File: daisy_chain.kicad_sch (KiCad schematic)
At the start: 21 parts, among them U1 BQ79616PAPRQ1, U2 SM91502ALA-E, U3 SM91502ALA-E

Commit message: PCB[Grounding, Heat]: Added some more pours for heat considerations for bjt, stiched more vias for heat consideration on balanace resistors. SCH[Notes, Block Diagram]: Working on spelling and notes updates, started block diagram.
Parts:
- renumbered C39 to C37, C40 to C38, C37 to C39, C38 to C40, C42 to C41, C41 to C42, CR2 to CR1, CR1 to CR2, R40 to R39, R39 to R40, R43 to R41, R44 to R42, R41 to R43, R42 to R44, U3 to U2, U2 to U3
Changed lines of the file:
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@@
 		(in_pos_files yes)
 		(dnp no)
-		(property "Reference" "#PWR041"
+		(property "Reference" "#PWR048"
 			(at 58.42 50.8 0)
 			(hide yes)
@@
 			(project "bms_slave"
 				(path "/f9e05184-c88b-4a88-ae9c-ab2bdb32be7c/c5103ceb-5325-4a84-a025-9638a412984e/f0b77e72-3d76-4cd4-bd9c-26bca4deb7f1"
-					(reference "#PWR041")
+					(reference "#PWR048")
 					(unit 1)
 				)
@@
 		(dnp no)
 		(fields_autoplaced yes)
-		(property "Reference" "C39"
+		(property "Reference" "C37"
 			(at 127 58.4199 90)
 			(show_name no)
@@
 			(project "bms_slave"
 				(path "/f9e05184-c88b-4a88-ae9c-ab2bdb32be7c/c5103ceb-5325-4a84-a025-9638a412984e/f0b77e72-3d76-4cd4-bd9c-26bca4deb7f1"
-					(reference "C39")
+					(reference "C37")
 					(unit 1)
 				)
@@
 		(dnp no)
 		(fields_autoplaced yes)
-		(property "Reference" "#PWR044"
+		(property "Reference" "#PWR053"
 			(at 124.46 119.38 0)
 			(hide yes)
@@
 			(project "bms_slave"
 				(path "/f9e05184-c88b-4a88-ae9c-ab2bdb32be7c/c5103ceb-5325-4a84-a025-9638a412984e/f0b77e72-3d76-4cd4-bd9c-26bca4deb7f1"
-					(reference "#PWR044")
+					(reference "#PWR053")
 					(unit 1)
 				)
@@
 		(dnp no)
 		(fields_autoplaced yes)
-		(property "Reference" "#PWR045"
+		(property "Reference" "#PWR054"
 			(at 124.46 139.7 0)
 			(hide yes)
@@
 			(project "bms_slave"
 				(path "/f9e05184-c88b-4a88-ae9c-ab2bdb32be7c/c5103ceb-5325-4a84-a025-9638a412984e/f0b77e72-3d76-4cd4-bd9c-26bca4deb7f1"
-					(reference "#PWR045")
+					(reference "#PWR054")
 					(unit 1)
 				)
@@
 		(dnp no)
 		(fields_autoplaced yes)
-		(property "Reference" "#PWR048"
+		(property "Reference" "#PWR056"
 			(at 165.1 119.38 0)
 			(hide yes)
@@
 			(project "bms_slave"
 				(path "/f9e05184-c88b-4a88-ae9c-ab2bdb32be7c/c5103ceb-5325-4a84-a025-9638a412984e/f0b77e72-3d76-4cd4-bd9c-26bca4deb7f1"
-					(reference "#PWR048")
+					(reference "#PWR056")
 					(unit 1)
 				)
@@
 		(dnp no)
 		(fields_autoplaced yes)
-		(property "Reference" "U2"
+		(property "Reference" "U3"
 			(at 203.2 97.79 0)
 			(show_name no)
@@
 			(project "bms_slave"
 				(path "/f9e05184-c88b-4a88-ae9c-ab2bdb32be7c/c5103ceb-5325-4a84-a025-9638a412984e/f0b77e72-3d76-4cd4-bd9c-26bca4deb7f1"
-					(reference "U2")
+					(reference "U3")
 					(unit 1)
 				)
@@
 		(in_pos_files yes)
 		(dnp no)
-		(property "Reference" "CR2"
+		(property "Reference" "CR1"
 			(at 153.67 57.15 0)
 			(show_name no)
@@
 			(project "bms_slave"
 				(path "/f9e05184-c88b-4a88-ae9c-ab2bdb32be7c/c5103ceb-5325-4a84-a025-9638a412984e/f0b77e72-3d76-4cd4-bd9c-26bca4deb7f1"
-					(reference "CR2")
+					(reference "CR1")
 					(unit 1)
 				)
@@
 		(dnp no)
 		(fields_autoplaced yes)
-		(property "Reference" "C40"
+		(property "Reference" "C38"
 			(at 127 78.7399 90)
 			(show_name no)
@@
 			(project "bms_slave"
 				(path "/f9e05184-c88b-4a88-ae9c-ab2bdb32be7c/c5103ceb-5325-4a84-a025-9638a412984e/f0b77e72-3d76-4cd4-bd9c-26bca4deb7f1"
-					(reference "C40")
+					(reference "C38")
 					(unit 1)
 				)
@@
 		(dnp no)
 		(fields_autoplaced yes)
-		(property "Reference" "C37"
+		(property "Reference" "C39"
 			(at 127 105.4099 90)
 			(show_name no)
@@
 			(project "bms_slave"
 				(path "/f9e05184-c88b-4a88-ae9c-ab2bdb32be7c/c5103ceb-5325-4a84-a025-9638a412984e/f0b77e72-3d76-4cd4-bd9c-26bca4deb7f1"
-					(reference "C37")
+					(reference "C39")
 					(unit 1)
 				)
@@
 		(in_pos_files yes)
 		(dnp no)
-		(property "Reference" "R39"
+		(property "Reference" "R40"
 			(at 116.84 107.9499 90)
 			(show_name no)
@@
 			(project "bms_slave"
 				(path "/f9e05184-c88b-4a88-ae9c-ab2bdb32be7c/c5103ceb-5325-4a84-a025-9638a412984e/f0b77e72-3d76-4cd4-bd9c-26bca4deb7f1"
-					(reference "R39")
+					(reference "R40")
 					(unit 1)
 				)
@@
 		(in_pos_files yes)
 		(dnp no)
-		(property "Reference" "C42"
+		(property "Reference" "C41"
 			(at 171.45 59.69 0)
 			(show_name no)
@@
 			(project "bms_slave"
 				(path "/f9e05184-c88b-4a88-ae9c-ab2bdb32be7c/c5103ceb-5325-4a84-a025-9638a412984e/f0b77e72-3d76-4cd4-bd9c-26bca4deb7f1"
-					(reference "C42")
+					(reference "C41")
 					(unit 1)
 				)
@@
 		(dnp no)
 		(fields_autoplaced yes)
-		(property "Reference" "C38"
+		(property "Reference" "C40"
 			(at 127 125.7299 90)
 			(show_name no)
@@
 			(project "bms_slave"
 				(path "/f9e05184-c88b-4a88-ae9c-ab2bdb32be7c/c5103ceb-5325-4a84-a025-9638a412984e/f0b77e72-3d76-4cd4-bd9c-26bca4deb7f1"
-					(reference "C38")
+					(reference "C40")
 					(unit 1)
 				)
@@
 		(dnp no)
 		(fields_autoplaced yes)
-		(property "Reference" "#PWR047"
+		(property "Reference" "#PWR052"
 			(at 124.46 92.71 0)
 			(hide yes)
@@
 			(project "bms_slave"
 				(path "/f9e05184-c88b-4a88-ae9c-ab2bdb32be7c/c5103ceb-5325-4a84-a025-9638a412984e/f0b77e72-3d76-4cd4-bd9c-26bca4deb7f1"
-					(reference "#PWR047")
+					(reference "#PWR052")
 					(unit 1)
 				)
@@
 		(in_pos_files yes)
 		(dnp no)
-		(property "Reference" "C41"
+		(property "Reference" "C42"
 			(at 171.45 106.68 0)
 			(show_name no)
@@
 			(project "bms_slave"
 				(path "/f9e05184-c88b-4a88-ae9c-ab2bdb32be7c/c5103ceb-5325-4a84-a025-9638a412984e/f0b77e72-3d76-4cd4-bd9c-26bca4deb7f1"
-					(reference "C41")
+					(reference "C42")
 					(unit 1)
 				)
@@
 		(dnp no)
 		(fields_autoplaced yes)
-		(property "Reference" "R42"
+		(property "Reference" "R44"
 			(at 135.89 114.3 0)
 			(show_name no)
@@
 			(project "bms_slave"
 				(path "/f9e05184-c88b-4a88-ae9c-ab2bdb32be7c/c5103ceb-5325-4a84-a025-9638a412984e/f0b77e72-3d76-4cd4-bd9c-26bca4deb7f1"
-					(reference "R42")
+					(reference "R44")
 					(unit 1)
 				)
@@
 		(dnp no)
 		(fields_autoplaced yes)
-		(property "Reference" "R43"
+		(property "Reference" "R41"
 			(at 135.89 46.99 0)
 			(show_name no)
@@
 			(project "bms_slave"
 				(path "/f9e05184-c88b-4a88-ae9c-ab2bdb32be7c/c5103ceb-5325-4a84-a025-9638a412984e/f0b77e72-3d76-4cd4-bd9c-26bca4deb7f1"
-					(reference "R43")
+					(reference "R41")
 					(unit 1)
 				)
@@
 		(dnp no)
 		(fields_autoplaced yes)
-		(property "Reference" "#PWR046"
+		(property "Reference" "#PWR051"
 			(at 124.46 72.39 0)
 			(hide yes)
@@
 			(project "bms_slave"
 				(path "/f9e05184-c88b-4a88-ae9c-ab2bdb32be7c/c5103ceb-5325-4a84-a025-9638a412984e/f0b77e72-3d76-4cd4-bd9c-26bca4deb7f1"
-					(reference "#PWR046")
+					(reference "#PWR051")
 					(unit 1)
 				)
@@
 		(in_pos_files yes)
 		(dnp no)
-		(property "Reference" "R40"
+		(property "Reference" "R39"
 			(at 116.84 60.9599 90)
 			(show_name no)
@@
 			(project "bms_slave"
 				(path "/f9e05184-c88b-4a88-ae9c-ab2bdb32be7c/c5103ceb-5325-4a84-a025-9638a412984e/f0b77e72-3d76-4cd4-bd9c-26bca4deb7f1"
-					(reference "R40")
+					(reference "R39")
 					(unit 1)
 				)
@@
 		(dnp no)
 		(fields_autoplaced yes)
-		(property "Reference" "#PWR049"
+		(property "Reference" "#PWR055"
 			(at 165.1 72.39 0)
 			(hide yes)
@@
 			(project "bms_slave"
 				(path "/f9e05184-c88b-4a88-ae9c-ab2bdb32be7c/c5103ceb-5325-4a84-a025-9638a412984e/f0b77e72-3d76-4cd4-bd9c-26bca4deb7f1"
-					(reference "#PWR049")
+					(reference "#PWR055")
 					(unit 1)
 				)
@@
 		(in_pos_files yes)
 		(dnp no)
-		(property "Reference" "CR1"
+		(property "Reference" "CR2"
 			(at 153.67 104.14 0)
 			(show_name no)
@@
 			(project "bms_slave"
 				(path "/f9e05184-c88b-4a88-ae9c-ab2bdb32be7c/c5103ceb-5325-4a84-a025-9638a412984e/f0b77e72-3d76-4cd4-bd9c-26bca4deb7f1"
-					(reference "CR1")
+					(reference "CR2")
 					(unit 1)
 				)
@@
 		(in_pos_files yes)
 		(dnp no)
-		(property "Reference" "#PWR042"
+		(property "Reference" "#PWR049"
 			(at 58.42 59.69 0)
 			(hide yes)
@@
 			(project "bms_slave"
 				(path "/f9e05184-c88b-4a88-ae9c-ab2bdb32be7c/c5103ceb-5325-4a84-a025-9638a412984e/f0b77e72-3d76-4cd4-bd9c-26bca4deb7f1"
-					(reference "#PWR042")
+					(reference "#PWR049")
 					(unit 1)
 				)
@@
 		(dnp no)
 		(fields_autoplaced yes)
-		(property "Reference" "R44"
+		(property "Reference" "R42"
 			(at 135.89 67.31 0)
 			(show_name no)
@@
 			(project "bms_slave"
 				(path "/f9e05184-c88b-4a88-ae9c-ab2bdb32be7c/c5103ceb-5325-4a84-a025-9638a412984e/f0b77e72-3d76-4cd4-bd9c-26bca4deb7f1"
-					(reference "R44")
+					(reference "R42")
 					(unit 1)
 				)
@@
 		(dnp no)
 		(fields_autoplaced yes)
-		(property "Reference" "R41"
+		(property "Reference" "R43"
 			(at 135.89 93.98 0)
 			(show_name no)
@@
 			(project "bms_slave"
 				(path "/f9e05184-c88b-4a88-ae9c-ab2bdb32be7c/c5103ceb-5325-4a84-a025-9638a412984e/f0b77e72-3d76-4cd4-bd9c-26bca4deb7f1"
-					(reference "R41")
+					(reference "R43")
 					(unit 1)
 				)
@@
 		(in_pos_files yes)
 		(dnp no)
-		(property "Reference" "#PWR043"
+		(property "Reference" "#PWR050"
 			(at 81.28 95.25 0)
 			(hide yes)
@@
 			(project "bms_slave"
 				(path "/f9e05184-c88b-4a88-ae9c-ab2bdb32be7c/c5103ceb-5325-4a84-a025-9638a412984e/f0b77e72-3d76-4cd4-bd9c-26bca4deb7f1"
-					(reference "#PWR043")
+					(reference "#PWR050")
 					(unit 1)
 				)
@@
 		(dnp no)
 		(fields_autoplaced yes)
-		(property "Reference" "U3"
+		(property "Reference" "U2"
 			(at 203.2 50.8 0)
 			(show_name no)
@@
 			(project "bms_slave"
 				(path "/f9e05184-c88b-4a88-ae9c-ab2bdb32be7c/c5103ceb-5325-4a84-a025-9638a412984e/f0b77e72-3d76-4cd4-bd9c-26bca4deb7f1"
-					(reference "U3")
+					(reference "U2")
 					(unit 1)
 				)

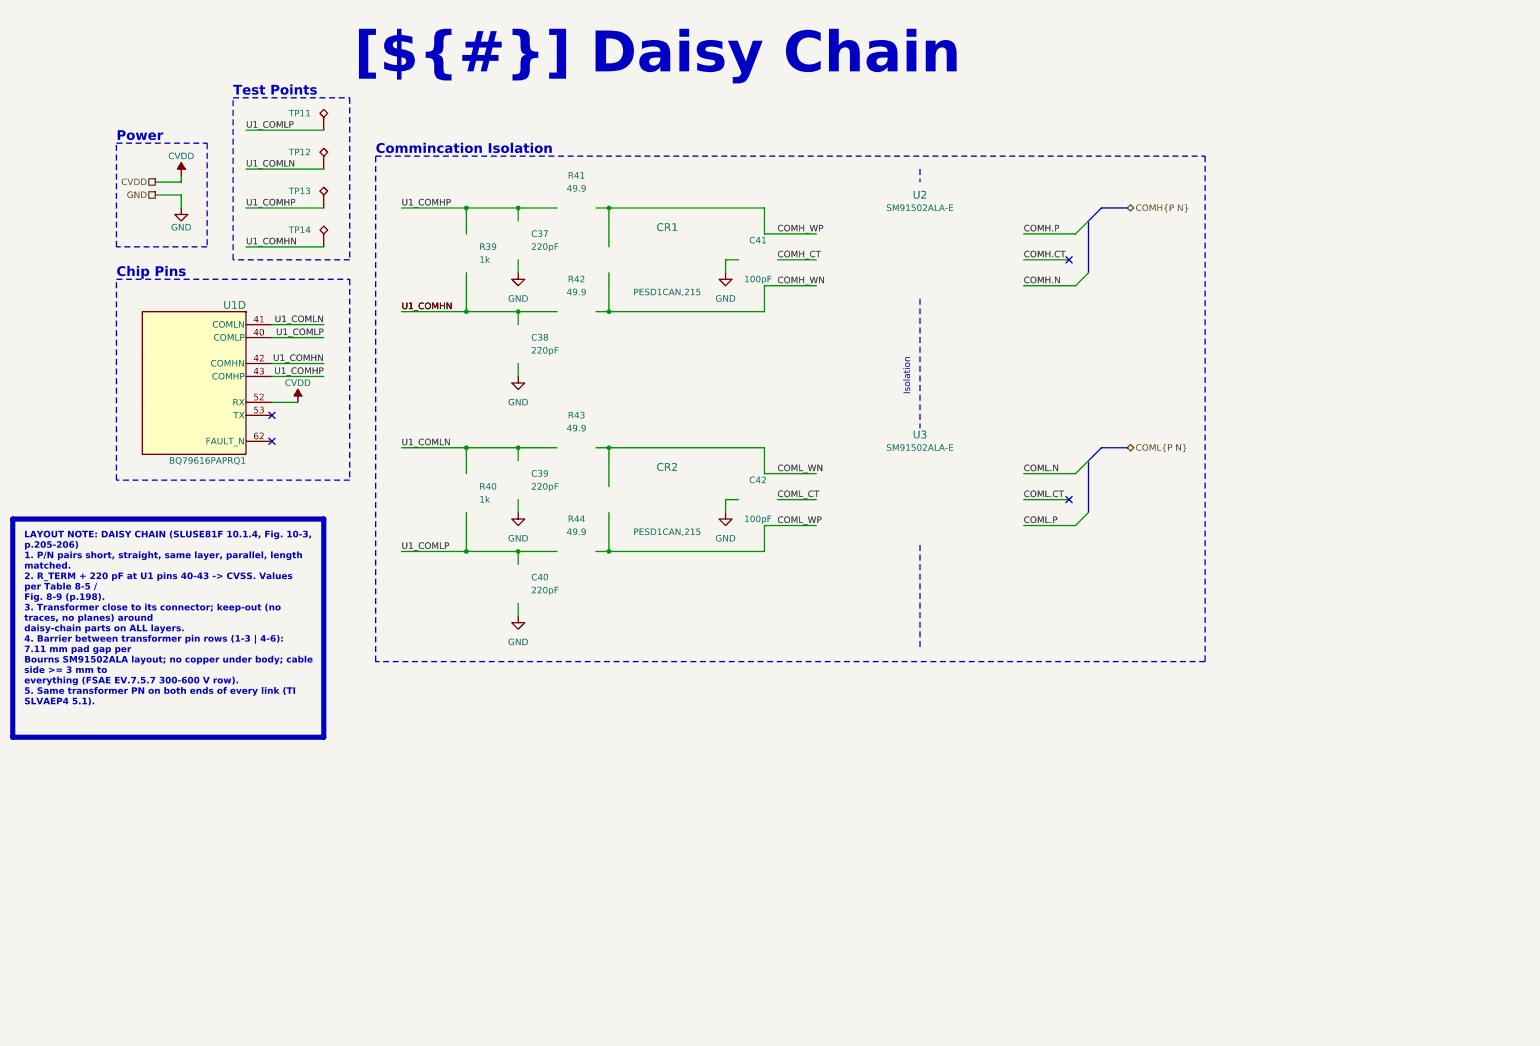
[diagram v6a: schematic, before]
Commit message: PCB[Test Points, Mechanical, Silk]: Finalized Mounting Points, Added Testpoints with adjecent silkscreen labels. SCH[Test Points, Notes]: Added/Updated notes for all pages, cleaned up errors spelling ect.
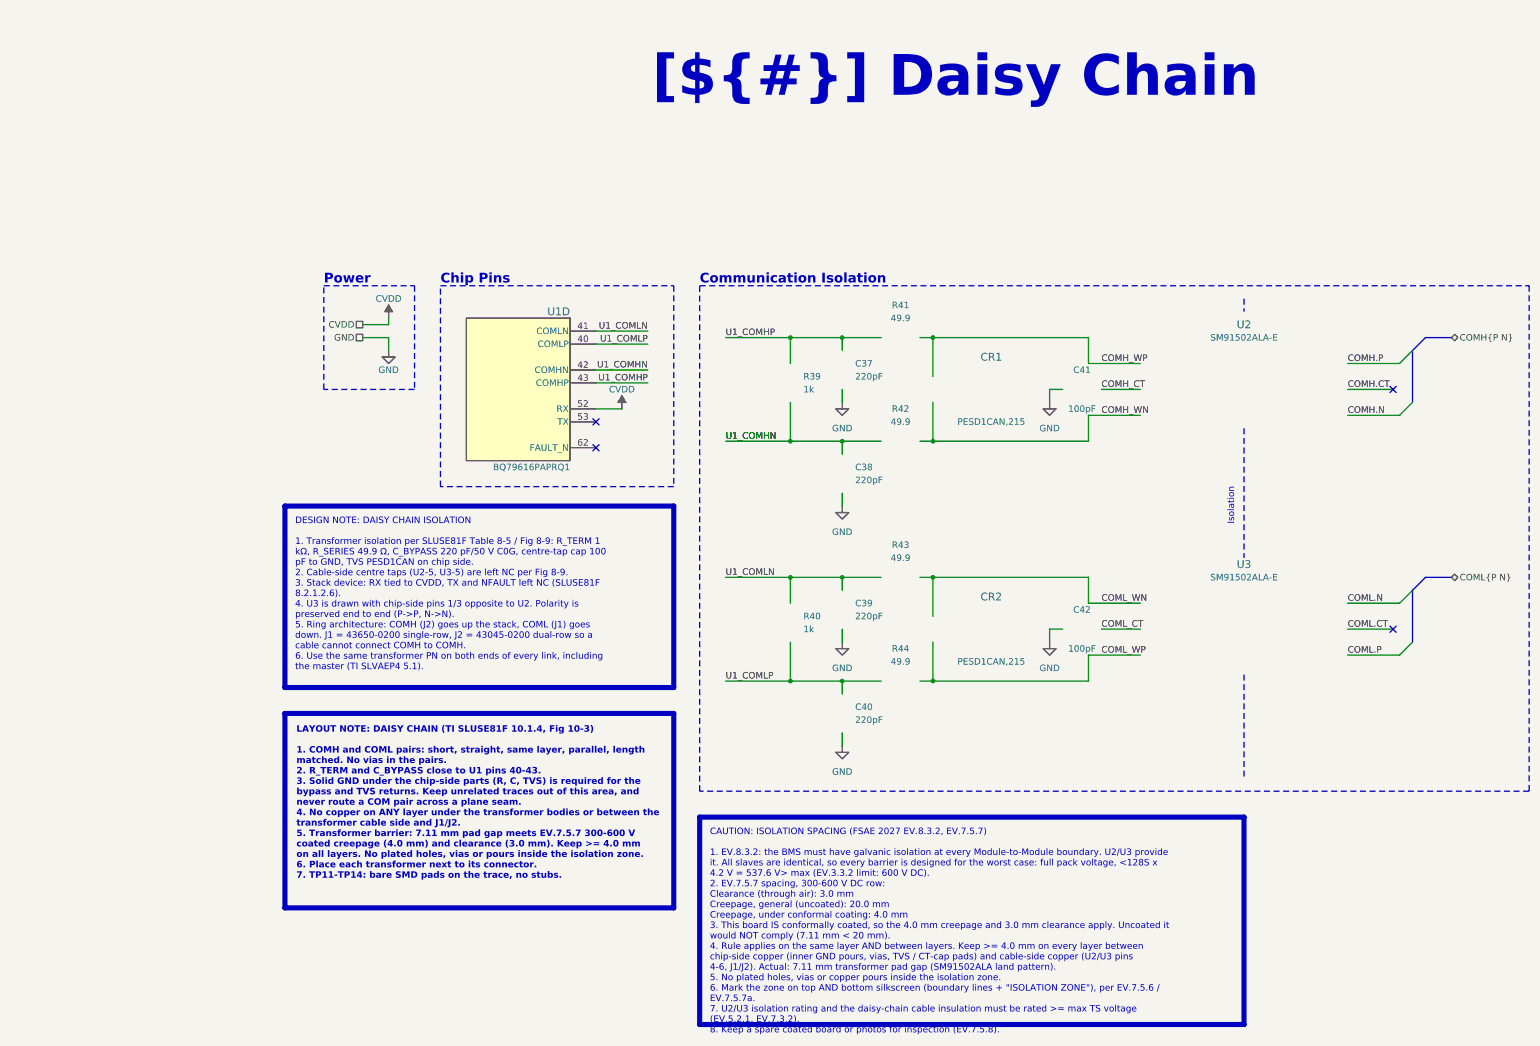
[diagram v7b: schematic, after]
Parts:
- removed TP11, TP12, TP13, TP14: (no value), TestPoint:TestPoint_Pad_D2.0mm, symbol Connector:TestPoint_Alt
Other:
- note added: "Communication Isolation"
- note removed: "Commincation Isolation"
- note removed: "Test Points"
- moved on the sheet: U1D

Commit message: PCB[Trace Size, Testpad, Daisy]: Changed Bat Trace size FAT, Made test pads larger, small trace movement to clean up, daisy trace change. SCH[Notes]: Small notes changes.
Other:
- company: (none) -> ${COMPANY}
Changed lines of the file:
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@@
 	(title_block
 		(title "Daisy Chain")
+		(date "2026-10-28")
+		(rev "${REVISION}")
+		(company "${COMPANY}")
 	)
 	(rectangle
@@
 		)
 	)
-	(text_box "DESIGN NOTE: DAISY CHAIN ISOLATION\n\n1. Transformer isolation per SLUSE81F Table 8-5 / Fig 8-9: R_TERM 1 kΩ, R_SERIES 49.9 Ω, C_BYPASS 220 pF/50 V C0G, centre-tap cap 100 pF to GND, TVS PESD1CAN on chip side.\n2. Cable-side centre taps (U2-5, U3-5) are left NC per Fig 8-9.\n3. Stack device: RX tied to CVDD, TX and NFAULT left NC (SLUSE81F 8.2.1.2.6).\n4. U3 is drawn with chip-side pins 1/3 opposite to U2. Polarity is preserved end to end (P->P, N->N).\n5. Ring architecture: COMH (J2) goes up the stack, COML (J1) goes down. J1 = 43650-0200 single-row, J2 = 43045-0200 dual-row so a cable cannot connect COMH to COMH.\n6. Use the same transformer PN on both ends of every link, including the master (TI SLVAEP4 5.1)."
+	(text_box "DESIGN NOTE: DAISY CHAIN ISOLATION\n\n1. Transformer isolation per Datasheet Table 8-5 / Fig 8-9: R_TERM 1 kΩ, R_SERIES 49.9 Ω, C_BYPASS 220 pF/50 V C0G, centre-tap cap 100 pF to GND, TVS PESD1CAN on chip side.\n2. Cable-side centre taps (U2-5, U3-5) are left NC per Fig 8-9.\n3. Stack device: RX tied to CVDD, TX and NFAULT left NC (Datasheet 8.2.1.2.6).\n4. U3 is drawn with chip-side pins 1/3 opposite to U2. Polarity is preserved end to end (P->P, N->N).\n5. Ring architecture: COMH (J2) goes up the stack, COML (J1) goes down. J1 = 43650-0200 single-row, J2 = 43045-0200 dual-row so a cable cannot connect COMH to COMH.\n6. Use the same transformer PN on both ends of every link, including the master (TI SLVAEP4 5.1)."
 		(exclude_from_sim no)
 		(at 78.74 111.76 0)
@@
 		)
 	)
-	(text_box "LAYOUT NOTE: DAISY CHAIN (TI SLUSE81F 10.1.4, Fig 10-3)\n\n1. COMH and COML pairs: short, straight, same layer, parallel, length matched. No vias in the pairs.\n2. R_TERM and C_BYPASS close to U1 pins 40-43.\n3. Solid GND under the chip-side parts (R, C, TVS) is required for the bypass and TVS returns. Keep unrelated traces out of this area, and never route a COM pair across a plane seam.\n4. No copper on ANY layer under the transformer bodies or between the transformer cable side and J1/J2.\n5. Transformer barrier: 7.11 mm pad gap meets EV.7.5.7 300-600 V coated creepage (4.0 mm) and clearance (3.0 mm). Keep >= 4.0 mm on all layers. No plated holes, vias or pours inside the isolation zone.\n6. Place each transformer next to its connector.\n7. TP11-TP14: bare SMD pads on the trace, no stubs."
+	(text_box "LAYOUT NOTE: DAISY CHAIN (TI Datasheet 10.1.4, Fig 10-3)\n\n1. COMH and COML pairs: short, straight, same layer, parallel, length matched. No vias in the pairs.\n2. R_TERM and C_BYPASS close to U1 pins 40-43.\n3. Solid GND under the chip-side parts (R, C, TVS) is required for the bypass and TVS returns. Keep unrelated traces out of this area, and never route a COM pair across a plane seam.\n4. No copper on ANY layer under the transformer bodies or between the transformer cable side and J1/J2.\n5. Transformer barrier: 7.11 mm pad gap meets EV.7.5.7 300-600 V coated creepage (4.0 mm) and clearance (3.0 mm). Keep >= 4.0 mm on all layers. No plated holes, vias or pours inside the isolation zone.\n6. Place each transformer next to its connector.\n7. TP11-TP14: bare SMD pads on the trace, no stubs."
 		(exclude_from_sim no)
 		(at 78.74 152.4 0)
